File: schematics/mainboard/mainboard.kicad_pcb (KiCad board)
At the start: 2 copper layers, 123.3 x 79.8 mm, 82 parts, among them J1 ICSP, J10 Conn_AGauge, J11 Conn_SAS, J2 USB_B_Micro, J3 DEALON DC-S050-200, J4 PWR_SELECT, J5 Conn_Joy1, J6 Conn_Joy2, J7 Conn_Throttle, J8 Conn_DGauges, J9 Conn_LCD, Q2 BC849, U1 ATmega2560-16A, U2 FT232RL, U3 USBLC6-2P6, U4 AIP78M05, U5 L9110, U6 74HC595, U7 74HC595, U8 74HC165, U9 74HC165, Y1 16Mhz

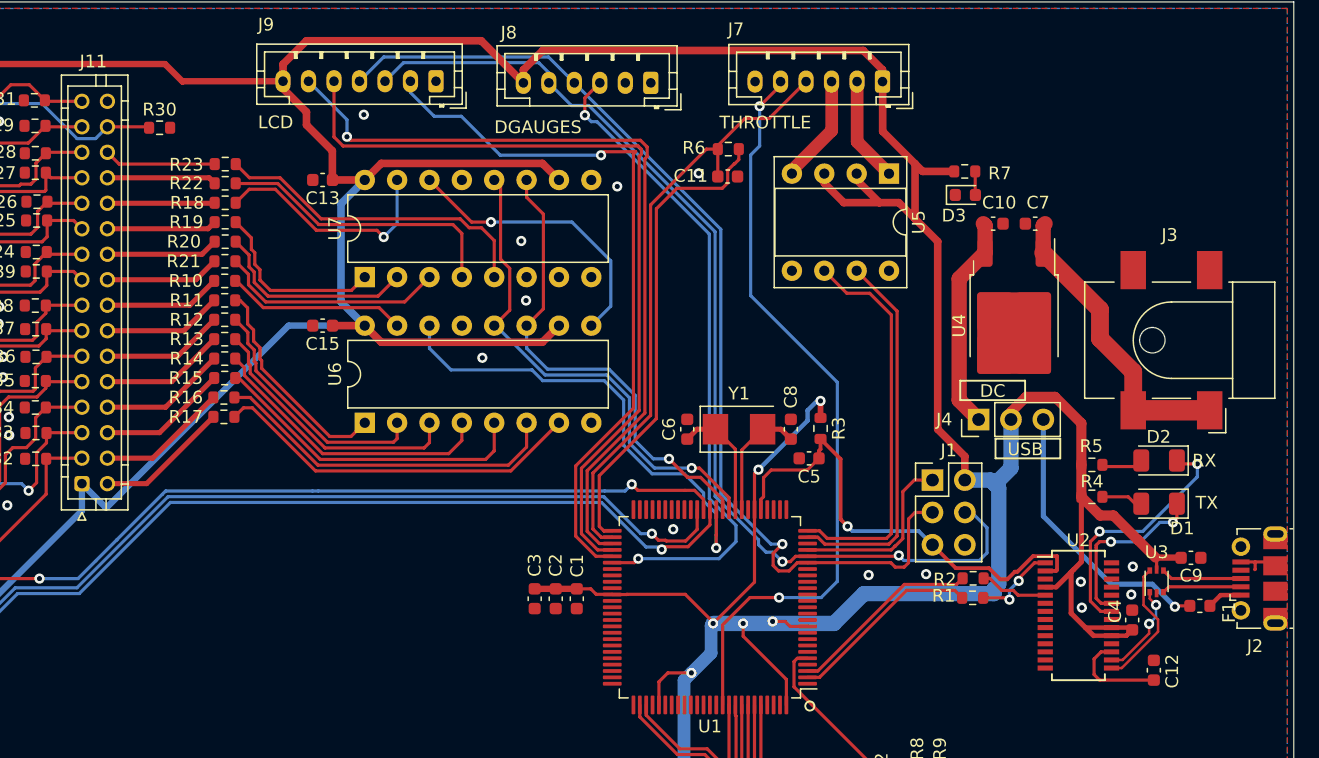
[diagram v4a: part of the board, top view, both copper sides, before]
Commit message: SCH:MB=> add pull-up to throttle signals
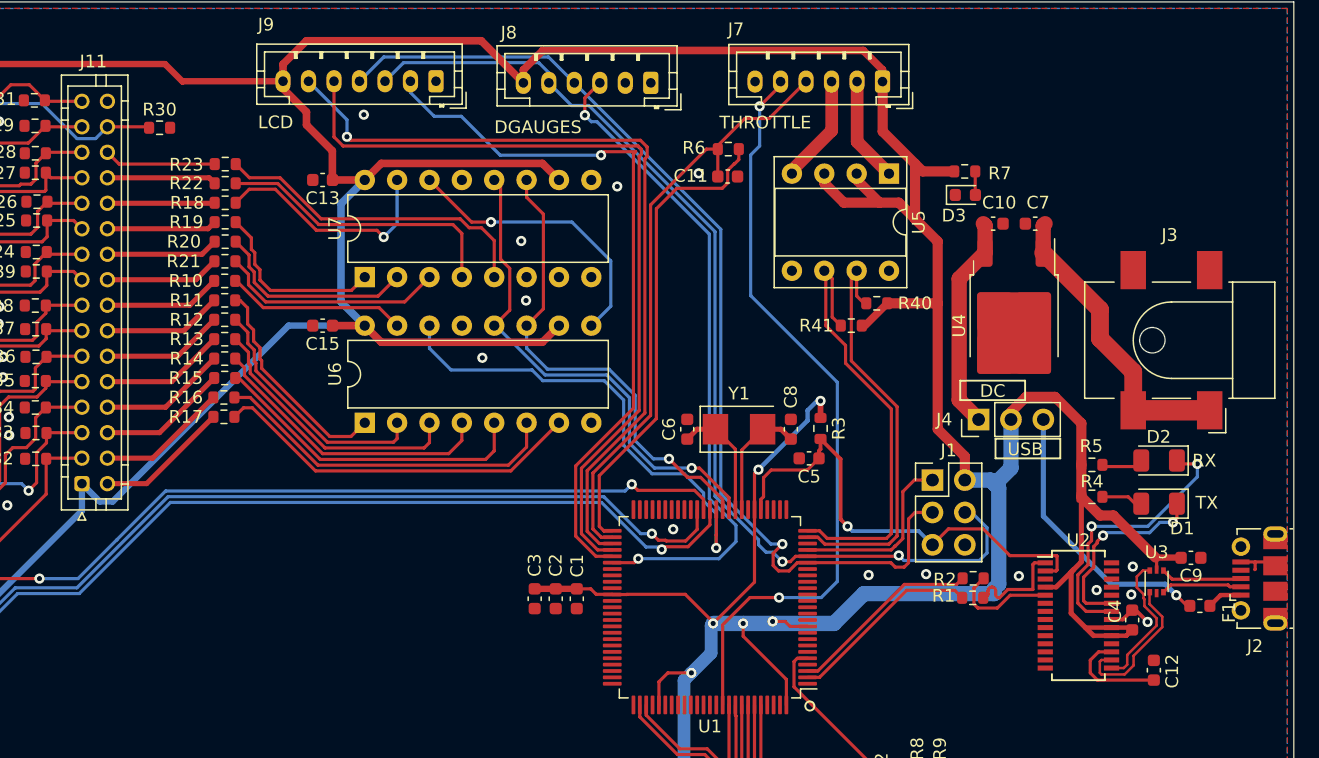
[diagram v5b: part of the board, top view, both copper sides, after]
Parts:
- added R40: 10K, Resistor_SMD:R_0603_1608Metric, F.Cu at (171.8, 46.0)
- added R41: 10K, Resistor_SMD:R_0603_1608Metric, F.Cu at (169.8, 47.8)
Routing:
- net +5V: track 457.7 -> 463.2 mm
- net /D-: track 7.48 -> 12.0 mm, vias 2 -> 0
- net /THROTTLE_DOWN: track 30.8 -> 34.6 mm
- net GND: track 3.44 -> 6.96 mm, vias 28 -> 29
- net /THROTTLE_UP: track 29.6 -> 33.0 mm
- net Net-(U2-RXD): track 5.38 -> 8.48 mm
- net Net-(D2-K): track 19.9 -> 22.0 mm
- net Net-(U2-TXD): track 6.66 -> 8.30 mm, vias 2 -> 0
- net Net-(D1-K): track 13.9 -> 15.5 mm
- net /D+: track 10.3 -> 11.1 mm

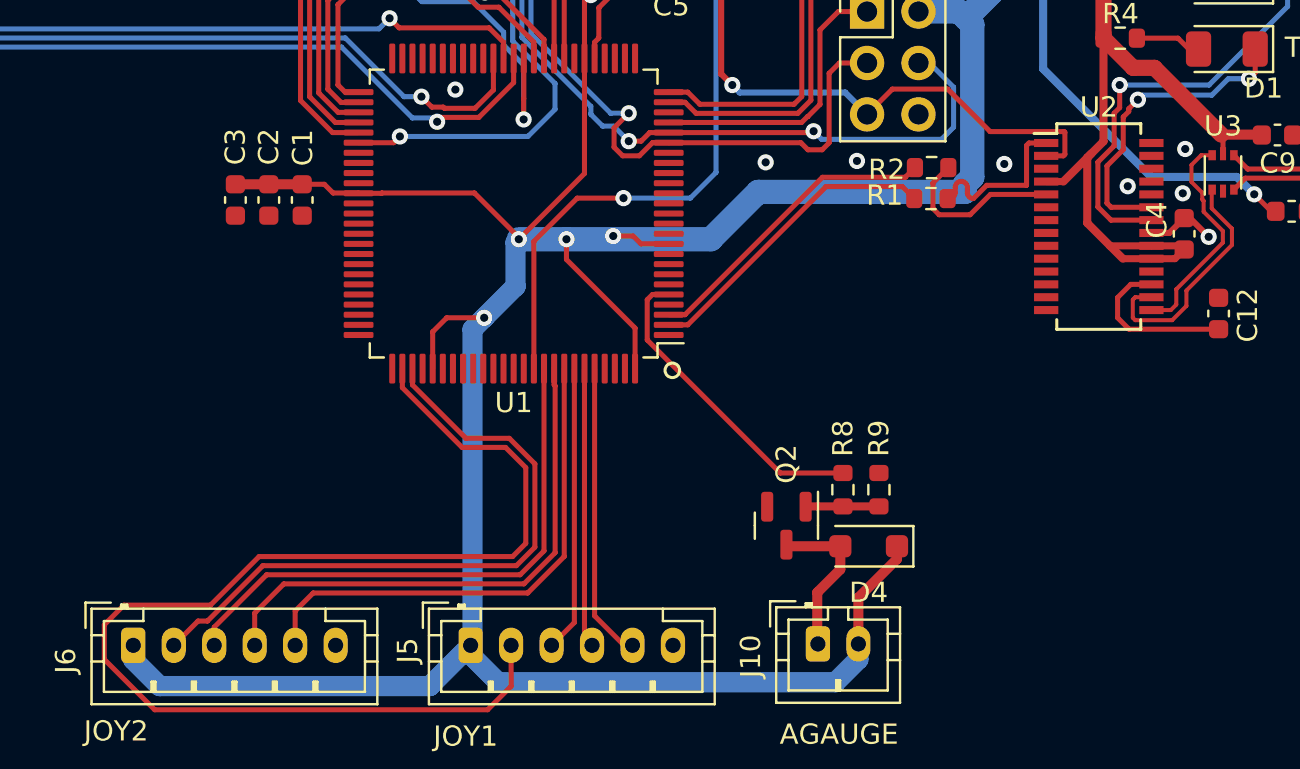
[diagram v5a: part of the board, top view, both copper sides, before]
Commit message: SCH:MB=> moved decoupling caps to each +5V on the ATMega
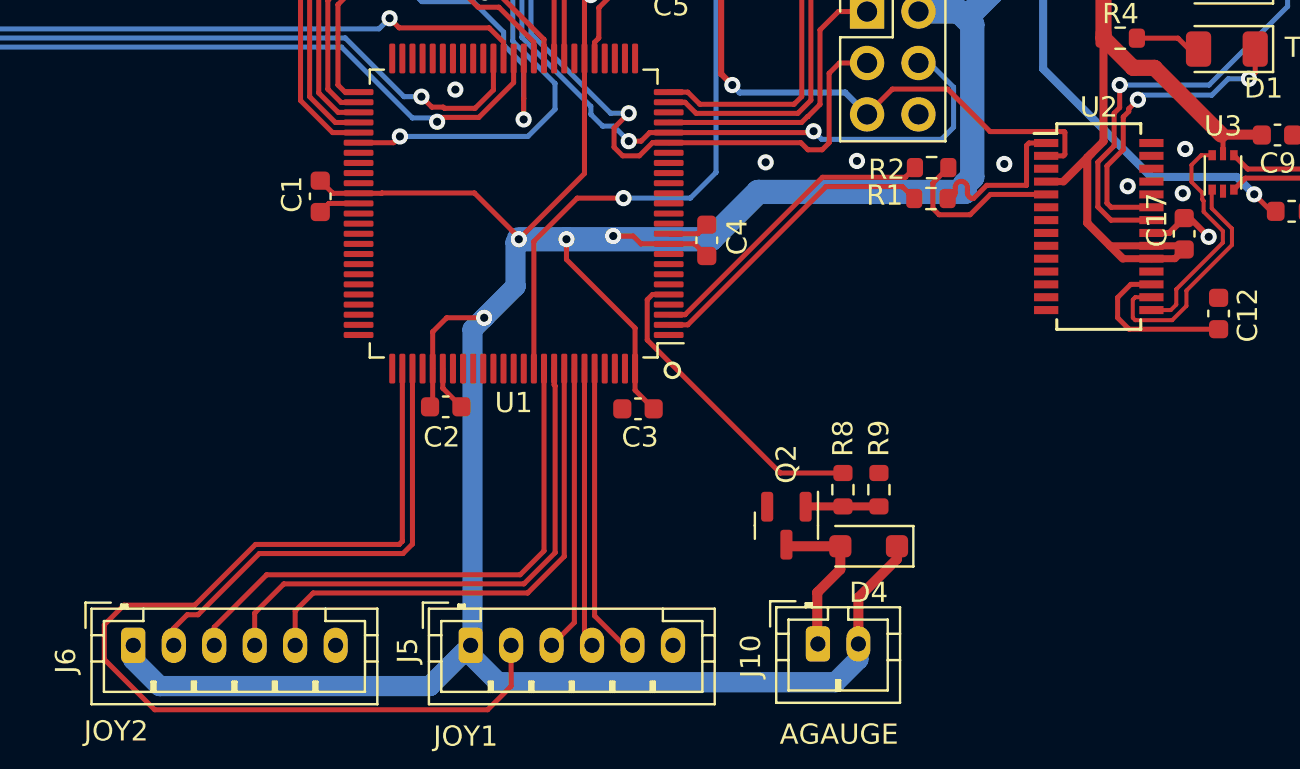
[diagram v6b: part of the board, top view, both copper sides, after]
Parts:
- added C4: 100nF, Capacitor_SMD:C_0603_1608Metric, F.Cu at (168.2, 71.2)
- moved C3 22.4 mm to (164.8, 79.5), turned to 180 degrees
- moved C2 13.4 mm to (155.3, 79.4), turned to 0 degrees
- moved C1 0.91 mm to (149.1, 69.0)
- renumbered C4 to C17
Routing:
- net /JOY1_PB: track 60.3 -> 50.3 mm
- net /JOY2_PB: track 32.4 -> 23.0 mm
- net GND: track 6.96 -> 13.4 mm
- net +5V: track 463.2 -> 465.5 mm

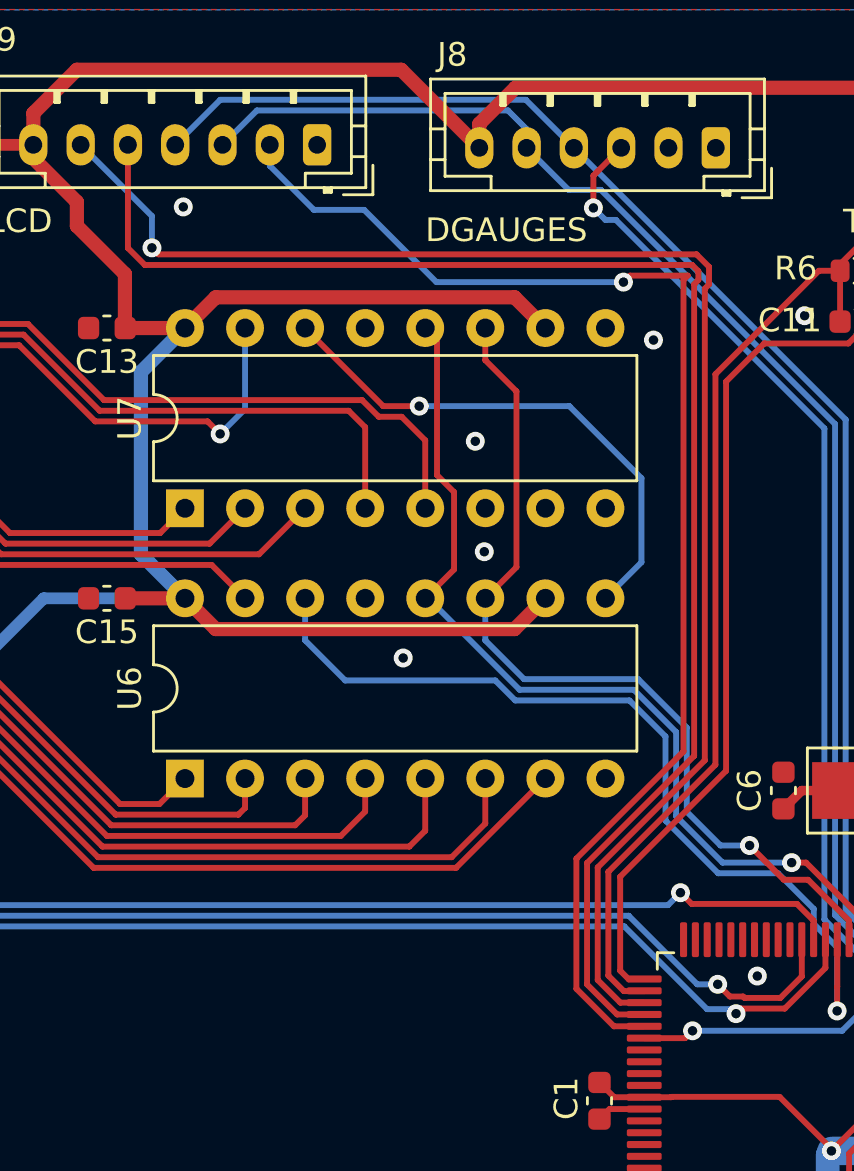
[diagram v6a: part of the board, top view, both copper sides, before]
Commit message: SCH: LCD => removed MB OE connection, now pulled to 3.3, always ON
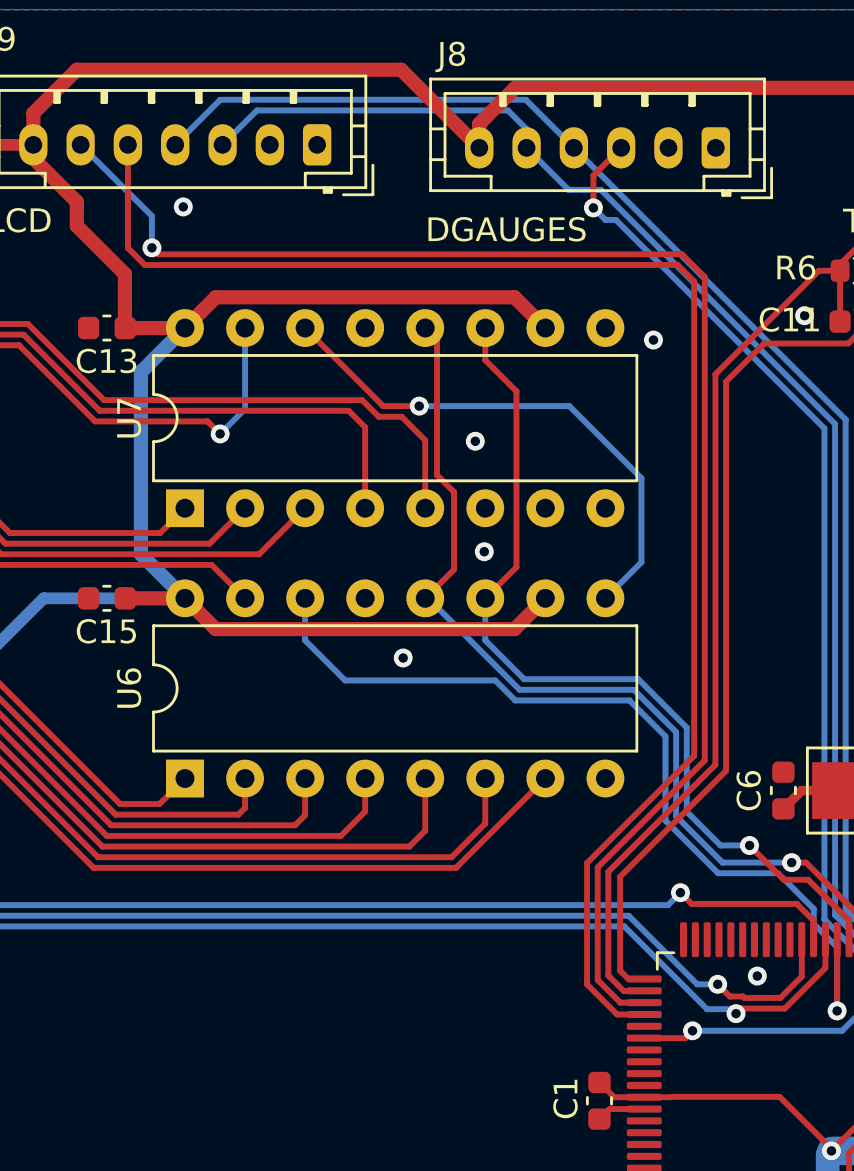
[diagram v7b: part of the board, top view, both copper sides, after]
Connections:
- J9 pad 2: Net-(J9-Pin_2) -> GND
- U1 pad 55: Net-(J9-Pin_2) -> unconnected-(U1-PC2-Pad55)
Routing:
- net Net-(J9-Pin_2): track 56.3 -> 0.00 mm, vias 1 -> 0
- net Net-(J9-Pin_6): track 64.0 -> 63.5 mm
- net Net-(J9-Pin_5): track 63.9 -> 63.4 mm
